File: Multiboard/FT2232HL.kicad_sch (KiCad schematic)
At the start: 41 parts, among them J5 Conn_01x06_Socket, U4 FT2232HL-REEL, U5 93LCxxC, Y3 12MHz

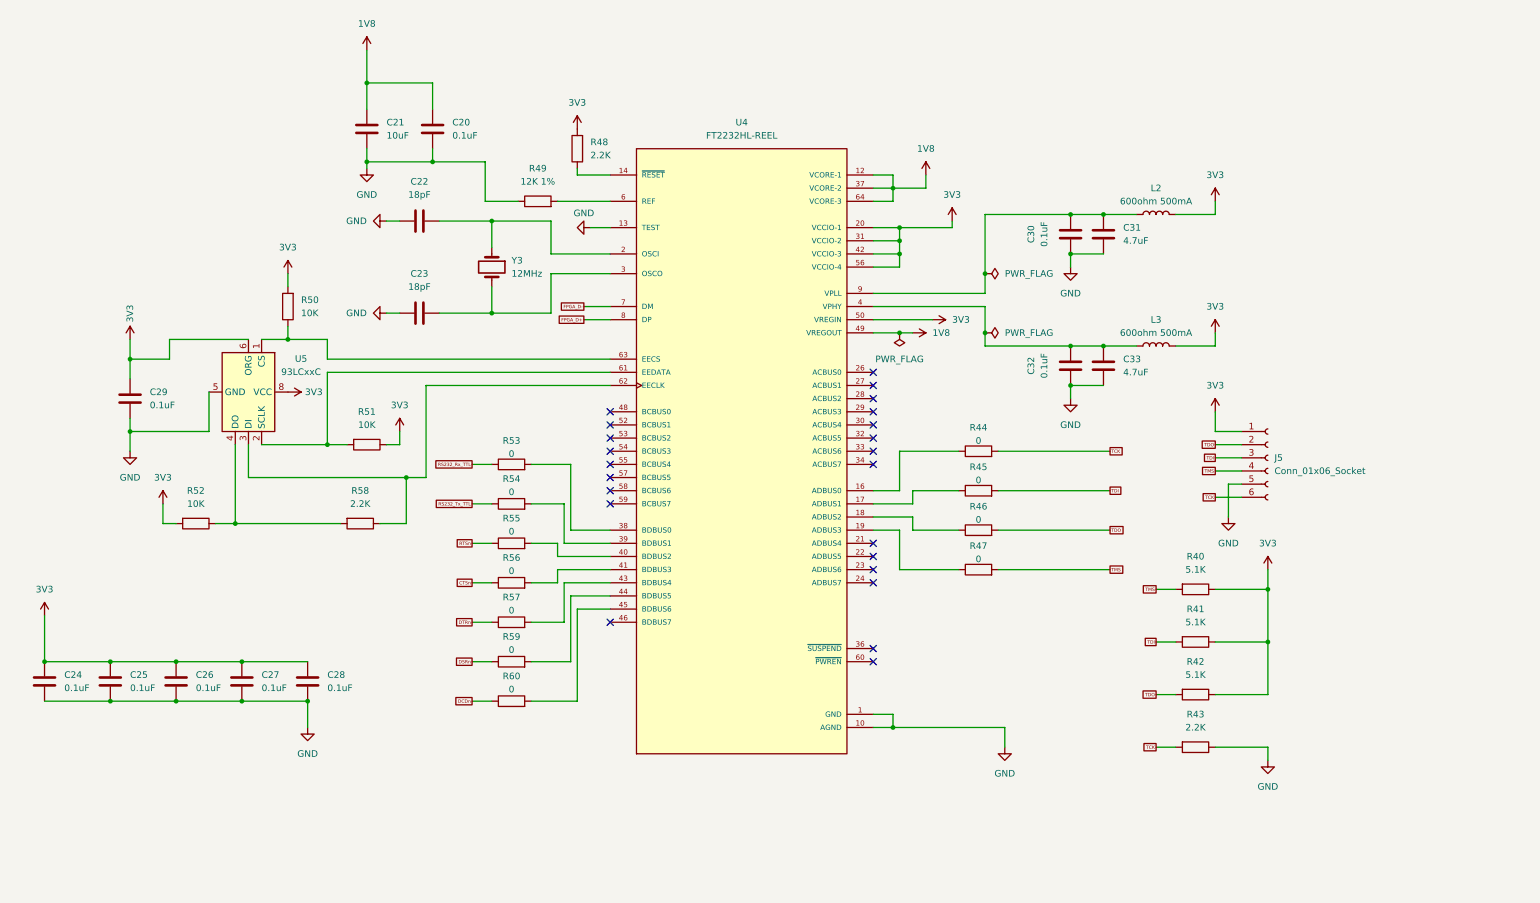
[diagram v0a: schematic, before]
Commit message: completed v1 FPGA schematic
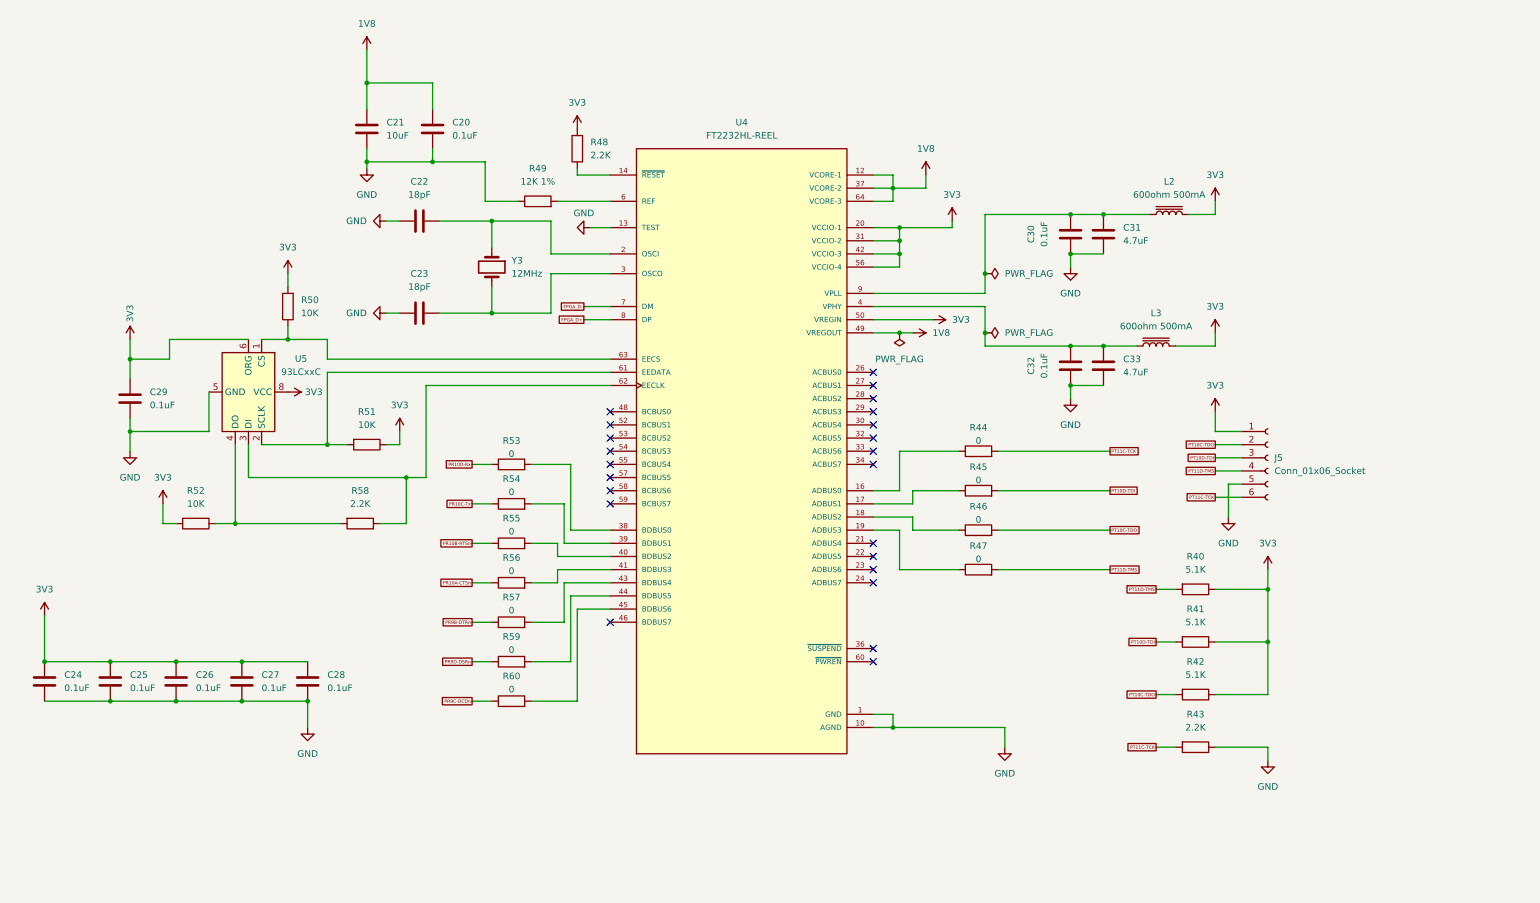
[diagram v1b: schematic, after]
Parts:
- removed L2, L3: 600ohm 500mA, symbol Device:L
- added L2, L3: 600ohm 500mA, Inductor_SMD:L_0603_1608Metric_Pad1.05x0.95mm_HandSolder, symbol Device:L_Iron
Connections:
- net 3V3: now also L2.2, L3.2
- net at C32.2, C33.2, U4.4 (VPHY): now also L3.1
- net at C30.2, C31.2, U4.9 (VPLL): now also L2.1
- net CTSn renamed PR10A-CTSn
- net DCDn renamed PR9C-DCDn
- net DSRn renamed PR9D-DSRn
- net DTRn renamed PR9B-DTRn
- net RS232_Rx_TTL renamed PR10D-Rx
- net RS232_Tx_TTL renamed PR10C-Tx
- net RTSn renamed PR10B-RTSn
- net TCK renamed PT11C-TCK
- net TDI renamed PT10D-TDI
- net TDO renamed PT10C-TDO
- net TMS renamed PT11D-TMS

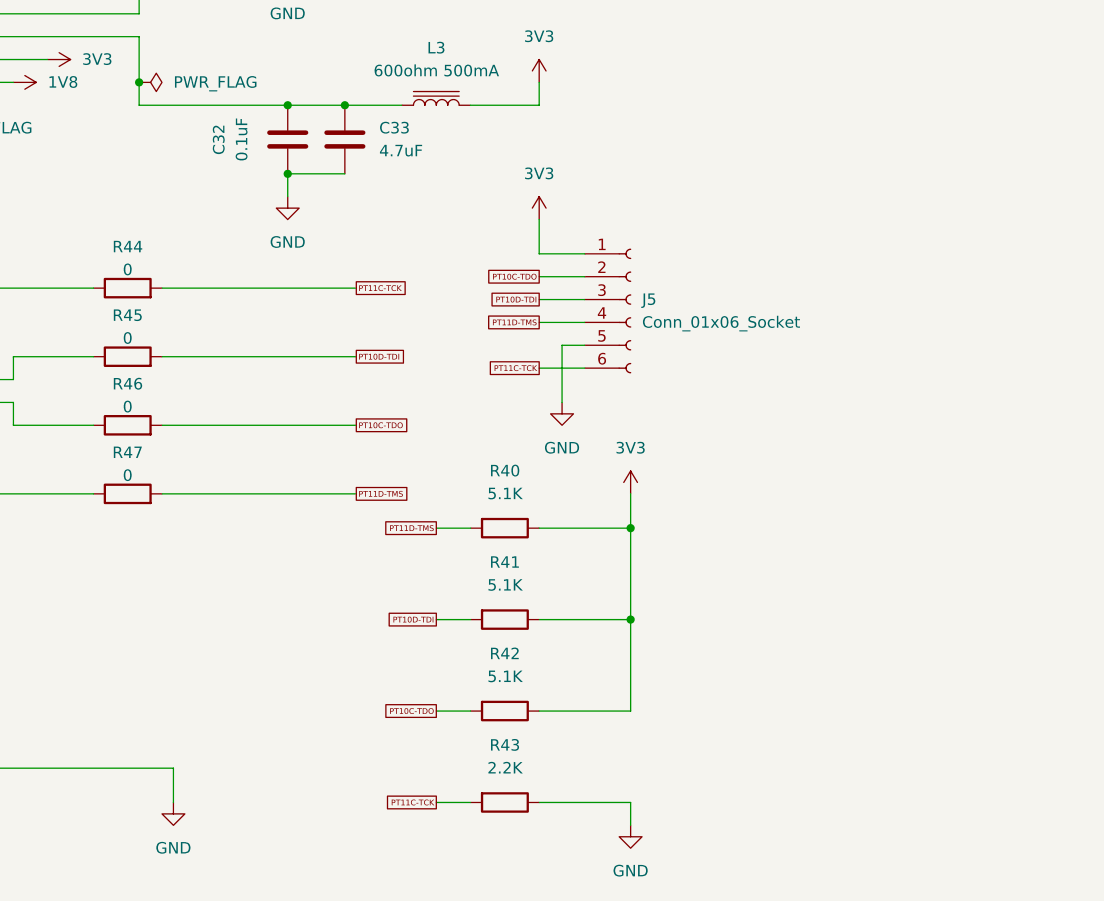
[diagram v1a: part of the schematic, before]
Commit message: Added footprints and fixed schematic
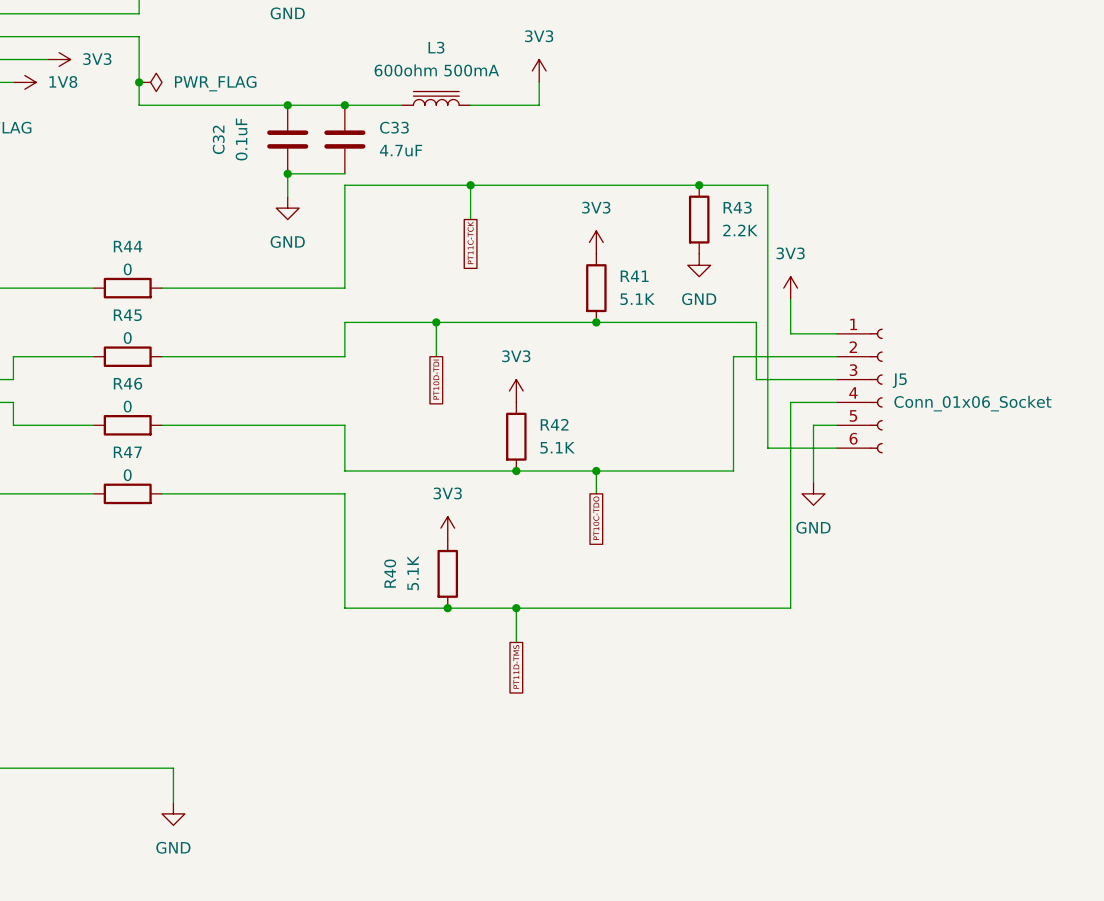
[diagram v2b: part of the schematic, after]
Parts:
- C20, C21, C22, C23, C24, C25, C26, C27, C28, C29, C30, C31, C32, C33: footprint (none) -> Capacitor_SMD:C_0603_1608Metric_Pad1.08x0.95mm_HandSolder
- J5: footprint (none) -> Connector_JST:JST_EH_S6B-EH_1x06_P2.50mm_Horizontal
- R40, R41, R42, R43, R44, R45, R46, R47, R48, R49, R50, R51, R52, R53, R54, R55, R56, R57, R58, R59, R60: footprint (none) -> Resistor_SMD:R_0603_1608Metric_Pad0.98x0.95mm_HandSolder
- U5: footprint (none) -> Package_SO:SO-8_3.9x4.9mm_P1.27mm
- Y3: footprint (none) -> Crystal:Crystal_SMD_TXC_7A-2Pin_5x3.2mm
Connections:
- net GND: now also R43.2; no longer R43.1
- net PT11C-TCK: now also R43.1; no longer R43.2
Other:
- moved on the sheet: J5, R40, R41, R42, R43

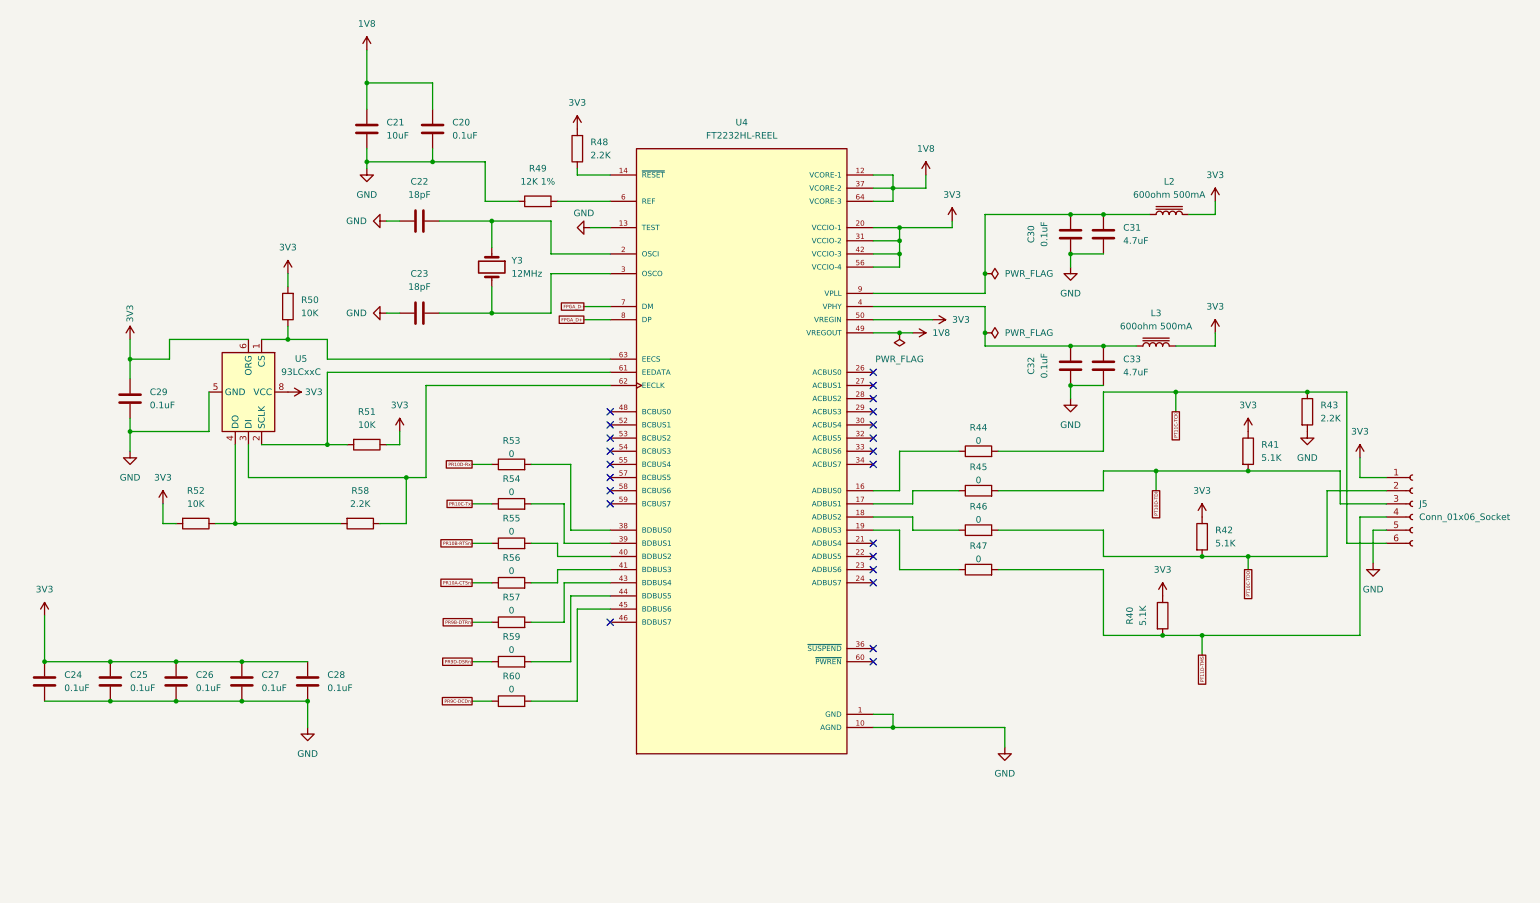
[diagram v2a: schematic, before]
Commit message: placed decoupling capacitors around fpga
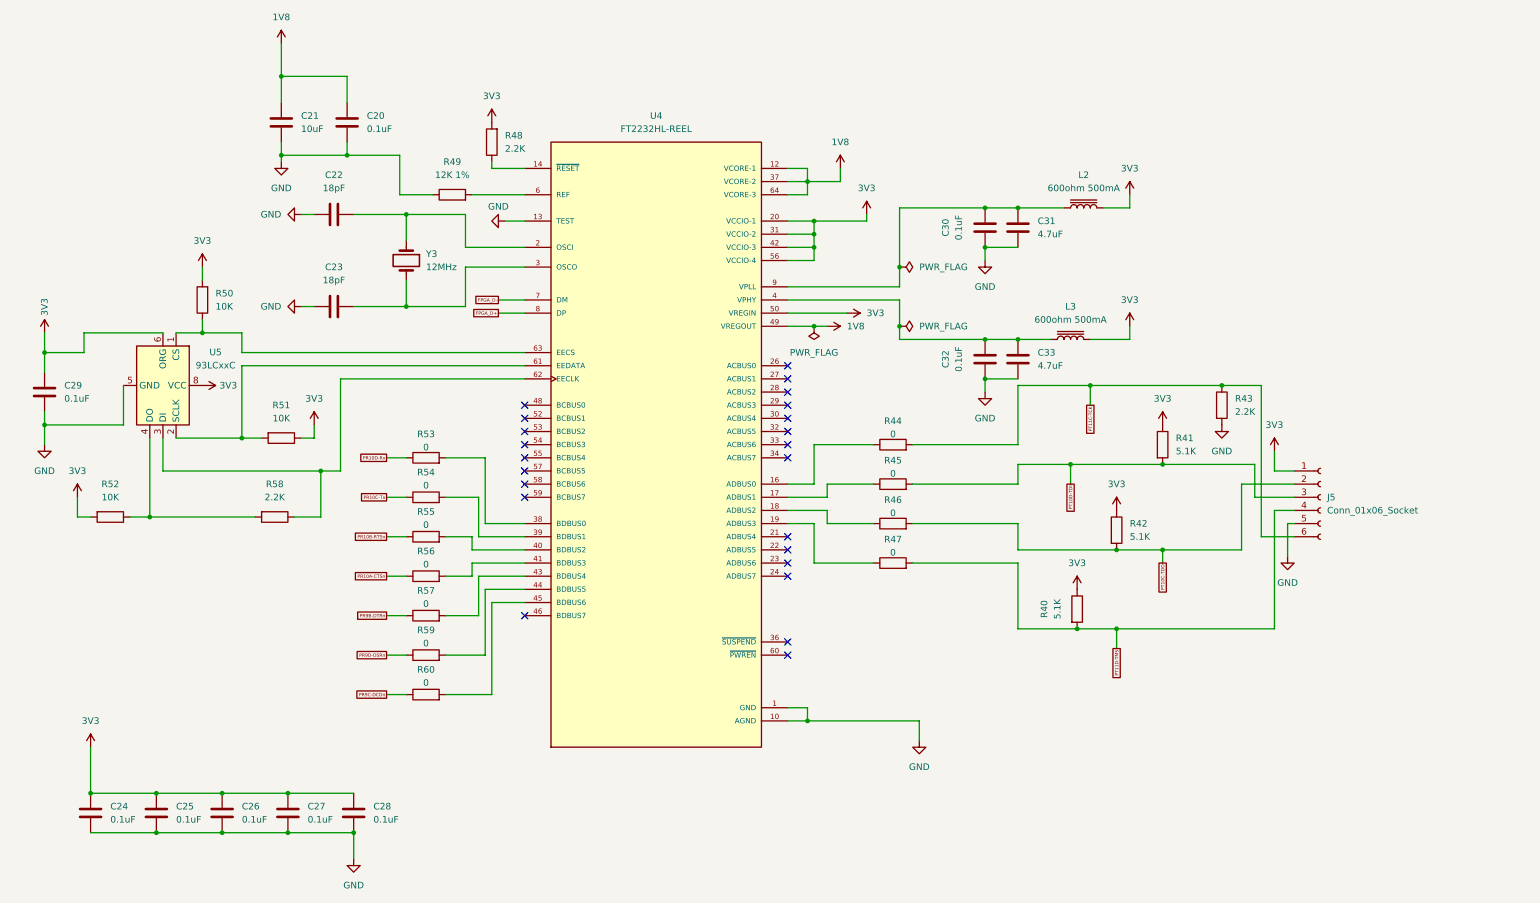
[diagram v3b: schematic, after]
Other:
- moved on the sheet: C20, C21, C22, C23, C24, C25, C26, C27, C28, C29, C30, C31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
